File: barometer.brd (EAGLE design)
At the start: 58.4 x 38.4 mm, 88 parts, among them IC1 MIC5225-3.3v, IC2 TPS5410, IC3 ZPA2326-0311A-R, U1 MCP4725, U2 LTC2850, U3 PCA9306, U4 MAX3221, U5 XC6215XC6215B182NR, U6 Tiny85-20-SMT, X2 1751264, X3 1751248

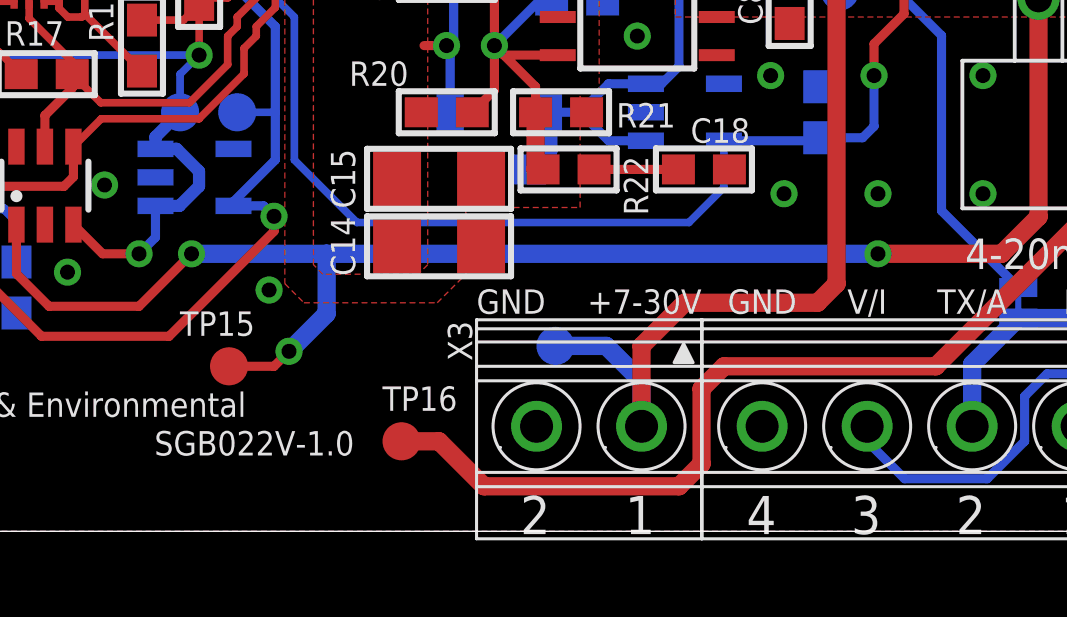
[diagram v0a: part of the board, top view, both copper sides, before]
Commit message: Displace test point from exclusion zone's periphery
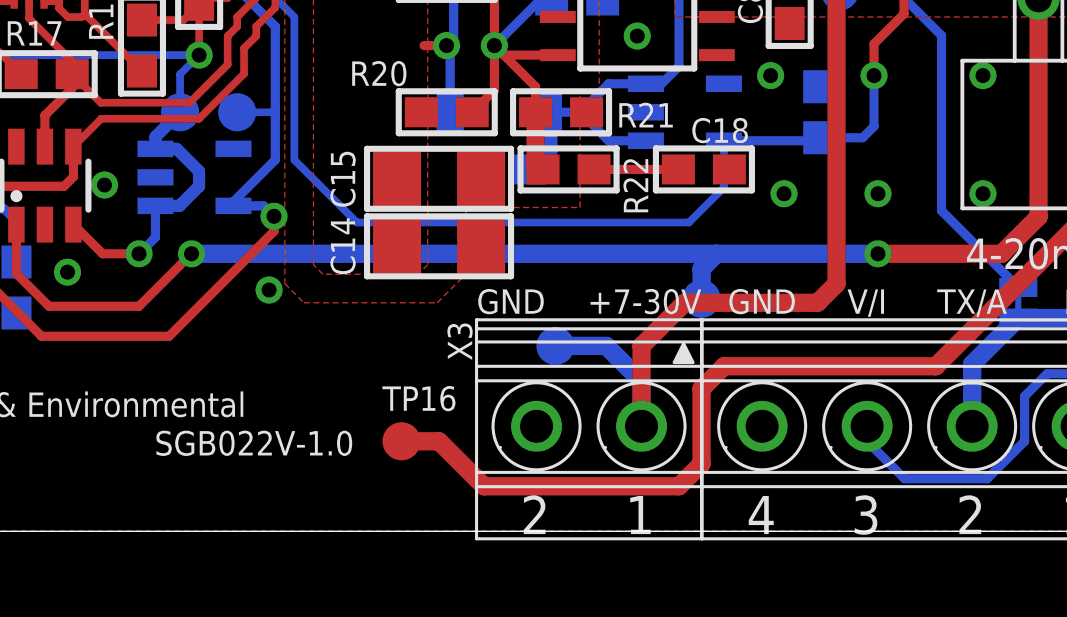
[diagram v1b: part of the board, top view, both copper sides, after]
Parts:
- moved TP15 15.9 mm to (36.8, 7.75), flipped to the bottom
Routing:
- net V-OUT: track 50.6 -> 46.4 mm, vias 3 -> 2
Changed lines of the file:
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@@
 <attribute name="NAME" x="23.7975" y="36.52" size="0.8128" layer="25" font="vector" ratio="18"/>
 </element>
-<element name="TP15" library="testpad" package="B1,27" value="PTR1B1,27" x="21" y="5.5" smashed="yes">
-<attribute name="TP_SIGNAL_NAME" value="" x="20.365" y="3.595" size="1" layer="37"/>
-<attribute name="NAME" x="19.365" y="6.516" size="0.8128" layer="25" font="vector" ratio="18"/>
+<element name="TP15" library="testpad" package="B1,27" value="PTR1B1,27" x="36.75" y="7.75" smashed="yes" rot="MR0">
+<attribute name="TP_SIGNAL_NAME" value="" x="37.385" y="5.845" size="1" layer="38" rot="MR0"/>
+<attribute name="NAME" x="38.385" y="8.766" size="0.8128" layer="26" font="vector" ratio="18" rot="MR0"/>
 </element>
 <element name="TP16" library="testpad" package="B1,27" value="PTR1B1,27" x="26.75" y="3" smashed="yes">
@@
 <via x="19.75" y="9.25" extent="1-16" drill="0.5"/>
 <contactref element="TP15" pad="TP"/>
-<wire x1="21" y1="5.5" x2="22.5" y2="5.5" width="0.3048" layer="1"/>
-<wire x1="22.5" y1="5.5" x2="23" y2="6" width="0.3048" layer="1"/>
-<via x="23" y="6" extent="1-16" drill="0.5"/>
 <contactref element="S-ANALOG" pad="P$2"/>
 <via x="42.63" y="9.25" extent="1-16" drill="0.5"/>
-<wire x1="42.63" y1="9.25" x2="24.25" y2="9.25" width="0.6096" layer="16"/>
-<wire x1="24.25" y1="9.25" x2="19.75" y2="9.25" width="0.6096" layer="16"/>
-<wire x1="23" y1="6" x2="24.25" y2="7.25" width="0.6096" layer="16"/>
-<wire x1="24.25" y1="7.25" x2="24.25" y2="9.25" width="0.6096" layer="16"/>
+<wire x1="42.63" y1="9.25" x2="37.25" y2="9.25" width="0.6096" layer="16"/>
+<wire x1="37.25" y1="9.25" x2="19.75" y2="9.25" width="0.6096" layer="16"/>
 <wire x1="42.63" y1="9.25" x2="46.75" y2="9.25" width="0.6096" layer="1"/>
 <wire x1="46.75" y1="9.25" x2="47.98375" y2="10.48375" width="0.6096" layer="1"/>
 <wire x1="47.98375" y1="10.48375" x2="47.98375" y2="17.75" width="0.6096" layer="1"/>
+<wire x1="36.75" y1="7.75" x2="36.75" y2="8.75" width="0.6096" layer="16"/>
+<wire x1="36.75" y1="8.75" x2="37.25" y2="9.25" width="0.6096" layer="16"/>
 </signal>
 <signal name="I-OUT">

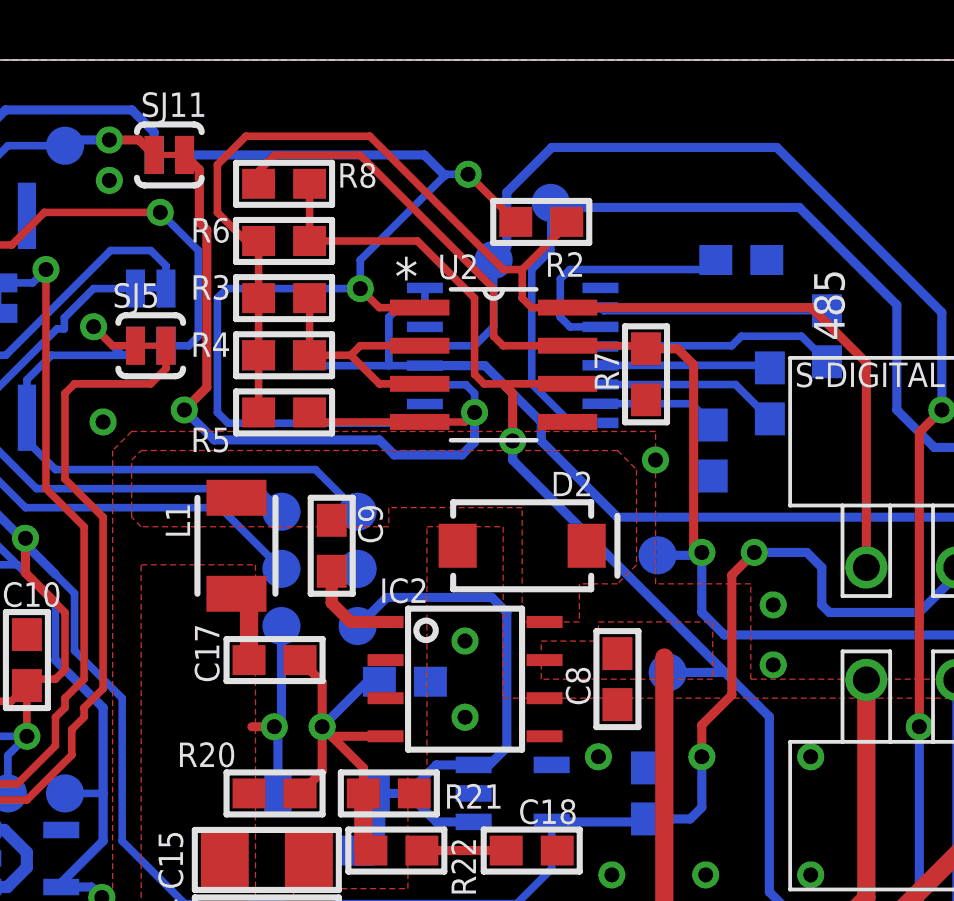
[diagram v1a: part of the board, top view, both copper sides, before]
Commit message: Add test point for 485 transmit/receive function control
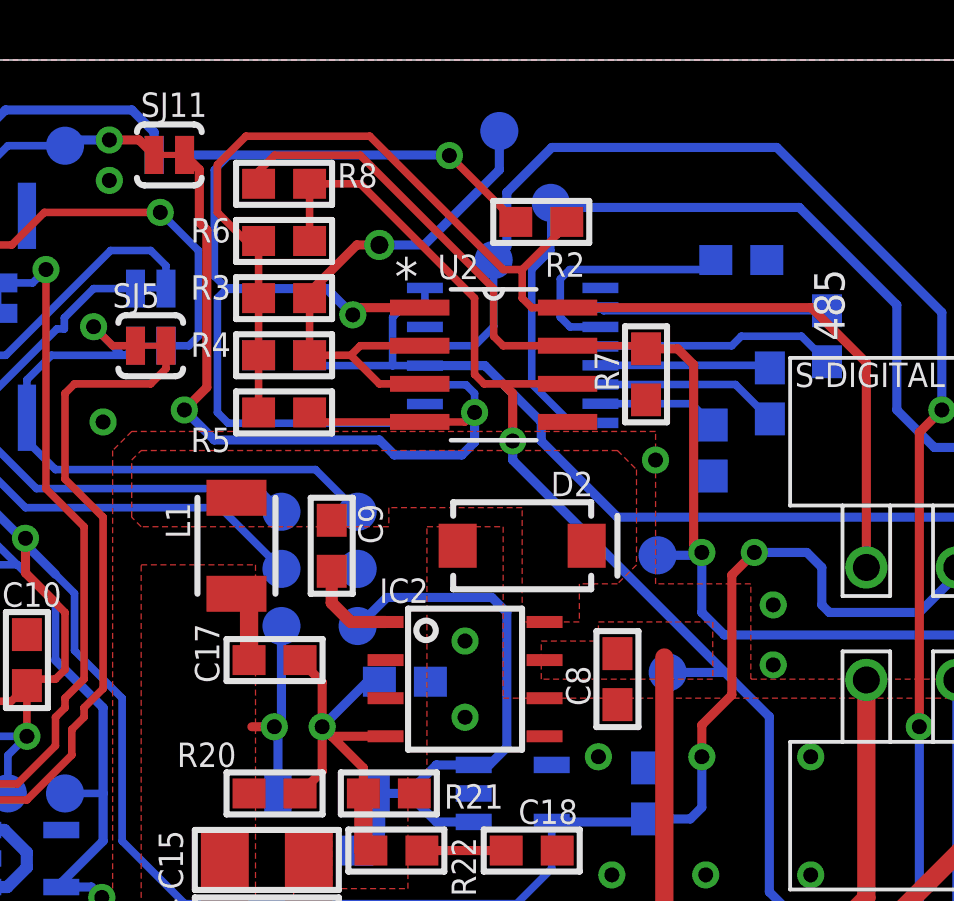
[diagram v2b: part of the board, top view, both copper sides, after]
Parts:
- added TP17: PTR1B1,27, testpad:B1,27
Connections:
- net 485EN: now also TP17.TP
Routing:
- net 485EN: track 8.40 -> 17.9 mm, vias 0 -> 1
- net A: track 40.1 -> 40.9 mm
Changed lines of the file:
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@@
 <element name="TP9" library="testpad" package="B1,27" value="PTR1B1,27" x="37.465" y="33.6525" smashed="yes" rot="MR0">
 <attribute name="TP_SIGNAL_NAME" value="" x="38.1" y="31.7475" size="1" layer="38" rot="MR0"/>
-<attribute name="NAME" x="38.1" y="34.6685" size="0.8128" layer="26" font="vector" ratio="18" rot="MR0"/>
+<attribute name="NAME" x="39.35" y="34.6685" size="0.8128" layer="26" font="vector" ratio="18" rot="MR0"/>
 </element>
 <element name="TP10" library="testpad" package="B1,27" value="PTR1B1,27" x="41.3625" y="18" smashed="yes" rot="MR0">
@@
 <element name="C15" library="microbuilder" package="1206" value="47u" x="28" y="11.75" smashed="yes">
 <attribute name="NAME" x="24.8" y="11.75" size="0.8128" layer="25" font="vector" ratio="18" rot="R90" align="center"/>
+</element>
+<element name="TP17" library="testpad" package="B1,27" value="PTR1B1,27" x="35.75" y="36.0475" smashed="yes" rot="MR0">
+<attribute name="TP_SIGNAL_NAME" value="" x="36.385" y="34.1425" size="1" layer="38" rot="MR0"/>
+<attribute name="NAME" x="34.76" y="36.1885" size="0.8128" layer="26" font="vector" ratio="18" rot="MR0"/>
 </element>
 </elements>
@@
 <contactref element="U2" pad="1"/>
 <contactref element="R2" pad="1"/>
-<wire x1="33.0962" y1="30.16" x2="31.75" y2="30.16" width="0.254" layer="1"/>
-<wire x1="31.75" y1="30.16" x2="31.115" y2="30.795" width="0.254" layer="1"/>
-<via x="31.115" y="30.795" extent="1-16" drill="0.5"/>
-<wire x1="31.115" y1="30.795" x2="31.115" y2="31.7475" width="0.254" layer="16"/>
-<wire x1="34.71" y1="34.605" x2="36.2975" y2="33.0175" width="0.254" layer="1"/>
-<via x="34.71" y="34.605" extent="1-16" drill="0.5"/>
-<wire x1="34.71" y1="34.605" x2="33.9725" y2="34.605" width="0.254" layer="16"/>
-<wire x1="33.9725" y1="34.605" x2="33.93375" y2="34.56625" width="0.254" layer="16"/>
-<wire x1="33.93375" y1="34.56625" x2="31.115" y2="31.7475" width="0.254" layer="16"/>
+<via x="30.865" y="29.92" extent="1-16" drill="0.5"/>
+<wire x1="34.085" y1="35.23" x2="36.2975" y2="33.0175" width="0.254" layer="1"/>
+<via x="34.085" y="35.23" extent="1-16" drill="0.5"/>
 <wire x1="33.27" y1="26.3075" x2="26.7125" y2="26.3075" width="0.254" layer="16"/>
 <wire x1="26.7125" y1="26.3075" x2="26.3525" y2="26.6675" width="0.254" layer="16"/>
 <wire x1="26.3525" y1="26.6675" x2="26.3525" y2="30.4775" width="0.254" layer="16"/>
 <wire x1="26.3525" y1="30.4775" x2="26.67" y2="30.795" width="0.254" layer="16"/>
-<wire x1="26.67" y1="30.795" x2="31.115" y2="30.795" width="0.254" layer="16"/>
 <contactref element="SJ10" pad="2"/>
-<wire x1="25.258" y1="35.25" x2="33.25" y2="35.25" width="0.3048" layer="16"/>
-<wire x1="33.25" y1="35.25" x2="33.93375" y2="34.56625" width="0.3048" layer="16"/>
+<wire x1="25.258" y1="35.25" x2="26.75" y2="35.25" width="0.3048" layer="16"/>
+<wire x1="26.75" y1="35.25" x2="34.065" y2="35.25" width="0.3048" layer="16"/>
+<wire x1="34.065" y1="35.25" x2="34.085" y2="35.23" width="0.3048" layer="16"/>
+<wire x1="26.25" y1="31.215" x2="26.67" y2="30.795" width="0.254" layer="16"/>
+<wire x1="26.25" y1="31.215" x2="26.25" y2="34.75" width="0.254" layer="16"/>
+<wire x1="26.25" y1="34.75" x2="26.75" y2="35.25" width="0.254" layer="16"/>
+<wire x1="26.67" y1="30.795" x2="29.99" y2="30.795" width="0.3048" layer="16"/>
+<wire x1="29.99" y1="30.795" x2="30.865" y2="29.92" width="0.3048" layer="16"/>
+<wire x1="33.0962" y1="30.16" x2="31.105" y2="30.16" width="0.3048" layer="1"/>
+<wire x1="31.105" y1="30.16" x2="30.865" y2="29.92" width="0.3048" layer="1"/>
 </signal>
 <signal name="DIN">
@@
 <contactref element="R8" pad="2"/>
 <wire x1="29.425" y1="32.3825" x2="29.425" y2="34.2875" width="0.254" layer="1"/>
-<wire x1="29.425" y1="32.3825" x2="33.02" y2="32.3825" width="0.254" layer="1"/>
-<wire x1="33.02" y1="32.3825" x2="34.925" y2="30.4775" width="0.254" layer="1"/>
 <wire x1="34.925" y1="30.4775" x2="34.925" y2="27.9375" width="0.254" layer="1"/>
 <wire x1="34.925" y1="27.9375" x2="35.2425" y2="27.62" width="0.254" layer="1"/>
@@
 <contactref element="SJ3" pad="2"/>
 <wire x1="35.8775" y1="27.62" x2="38.0238" y2="27.62" width="0.254" layer="1"/>
-<wire x1="44.75" y1="16.525" x2="43.3875" y2="17.8875" width="0.3048" layer="16"/>
+<wire x1="44.75" y1="16.525" x2="43.275" y2="18" width="0.3048" layer="16"/>
 <wire x1="43.275" y1="18" x2="36.195" y2="25.08" width="0.3048" layer="16"/>
 <wire x1="36.195" y1="25.08" x2="36.195" y2="25.715" width="0.3048" layer="16"/>
@@
 <wire x1="44.75" y1="10.683" x2="47.3075" y2="8.1255" width="0.3048" layer="16"/>
 <wire x1="41.3625" y1="18" x2="43.275" y2="18" width="0.3048" layer="16"/>
-<wire x1="43.275" y1="18" x2="43.3875" y2="17.8875" width="0.3048" layer="16"/>
+<wire x1="34.925" y1="30.4775" x2="31.115" y2="34.2875" width="0.254" layer="1"/>
+<wire x1="31.115" y1="34.2875" x2="29.425" y2="34.2875" width="0.254" layer="1"/>
 </signal>
 <signal name="B">
@@
 <contactref element="C7" pad="1"/>
 <wire x1="29.425" y1="28.5725" x2="29.77" y2="28.2275" width="0.254" layer="16"/>
-<wire x1="29.77" y1="28.2275" x2="32.0675" y2="28.2275" width="0.254" layer="16"/>
-<wire x1="32.0675" y1="28.2275" x2="33.27" y2="28.2275" width="0.254" layer="16"/>
+<wire x1="29.77" y1="28.2275" x2="32.1925" y2="28.2275" width="0.254" layer="16"/>
+<wire x1="32.1925" y1="28.2275" x2="33.27" y2="28.2275" width="0.254" layer="16"/>
 <wire x1="33.27" y1="30.1675" x2="33.27" y2="30.8175" width="0.254" layer="16"/>
-<wire x1="33.27" y1="30.1675" x2="32.3925" y2="30.1675" width="0.254" layer="16"/>
-<wire x1="32.3925" y1="30.1675" x2="32.0675" y2="29.8425" width="0.254" layer="16"/>
-<wire x1="32.0675" y1="29.8425" x2="32.0675" y2="28.2275" width="0.254" layer="16"/>
+<wire x1="33.27" y1="30.1675" x2="32.5175" y2="30.1675" width="0.254" layer="16"/>
+<wire x1="32.5175" y1="30.1675" x2="32.1925" y2="29.8425" width="0.254" layer="16"/>
+<wire x1="32.1925" y1="29.8425" x2="32.1925" y2="28.2275" width="0.254" layer="16"/>
 <wire x1="33.27" y1="28.2275" x2="35.27" y2="28.2275" width="0.3048" layer="16"/>
 <wire x1="35.27" y1="28.2275" x2="37.1475" y2="26.35" width="0.3048" layer="16"/>
@@
 <wire x1="33.0962" y1="28.89" x2="31.115" y2="28.89" width="0.254" layer="1"/>
 <wire x1="31.115" y1="28.89" x2="30.7975" y2="28.5725" width="0.254" layer="1"/>
+<contactref element="TP17" pad="TP"/>
+<wire x1="35.75" y1="36.0475" x2="35.75" y2="34.75" width="0.3048" layer="16"/>
+<wire x1="35.75" y1="34.75" x2="33.25" y2="32.25" width="0.3048" layer="16"/>
+<wire x1="33.25" y1="32.25" x2="31.75" y2="32.25" width="0.3048" layer="16"/>
+<via x="31.75" y="32.25" extent="1-16" drill="0.6"/>
+<wire x1="31.75" y1="32.25" x2="31" y2="32.25" width="0.3048" layer="1"/>
+<wire x1="31" y1="32.25" x2="29.425" y2="30.675" width="0.3048" layer="1"/>
+<wire x1="29.425" y1="30.675" x2="29.425" y2="30.4775" width="0.3048" layer="1"/>
 </signal>
 <signal name="485VCC">

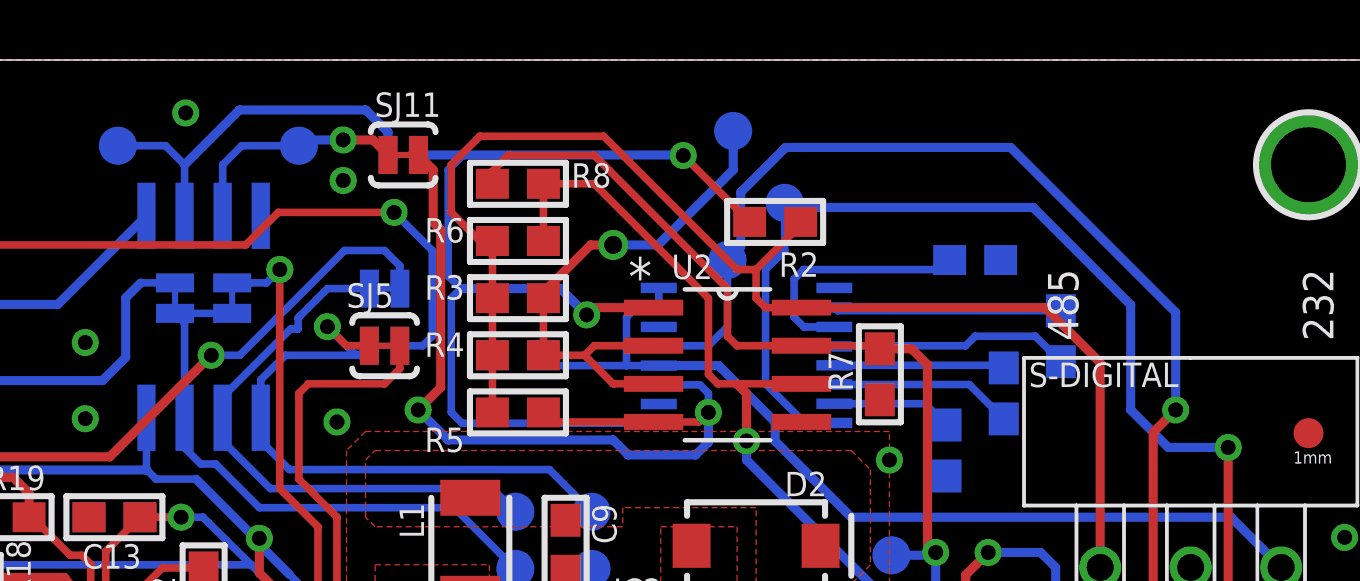
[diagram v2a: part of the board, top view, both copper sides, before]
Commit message: Integrate 485 transmit/receive function control with the microcontroller
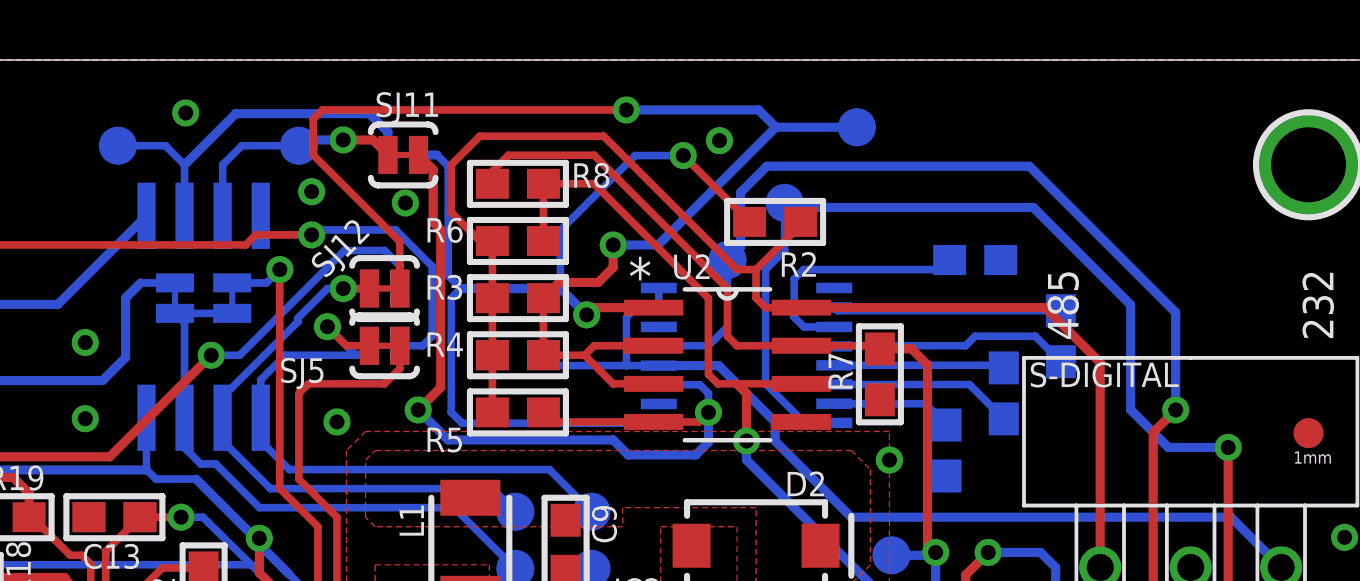
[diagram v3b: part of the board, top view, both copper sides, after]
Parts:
- added SJ12: SOLDERJUMPERTRACE, SparkFun-Retired:SJ_2S-TRACE
- moved TP17 4.13 mm to (39.9, 36.2)
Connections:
- net 485EN: now also SJ12.2
- net B1: now also SJ12.1
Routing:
- net 485EN: track 17.9 -> 44.5 mm, vias 1 -> 2
- net ROUT: track 35.0 -> 33.8 mm
- net MOSI: track 34.5 -> 33.8 mm
- net B1: track 19.7 -> 20.4 mm, vias 0 -> 1
- net DOUT: track 46.8 -> 46.3 mm
